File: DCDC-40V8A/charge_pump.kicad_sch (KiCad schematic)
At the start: 11 parts, among them Q23 2N7002, Q24 BSS83P, Q25 2N7002, U15 NE555D, U16 74LVC1G04

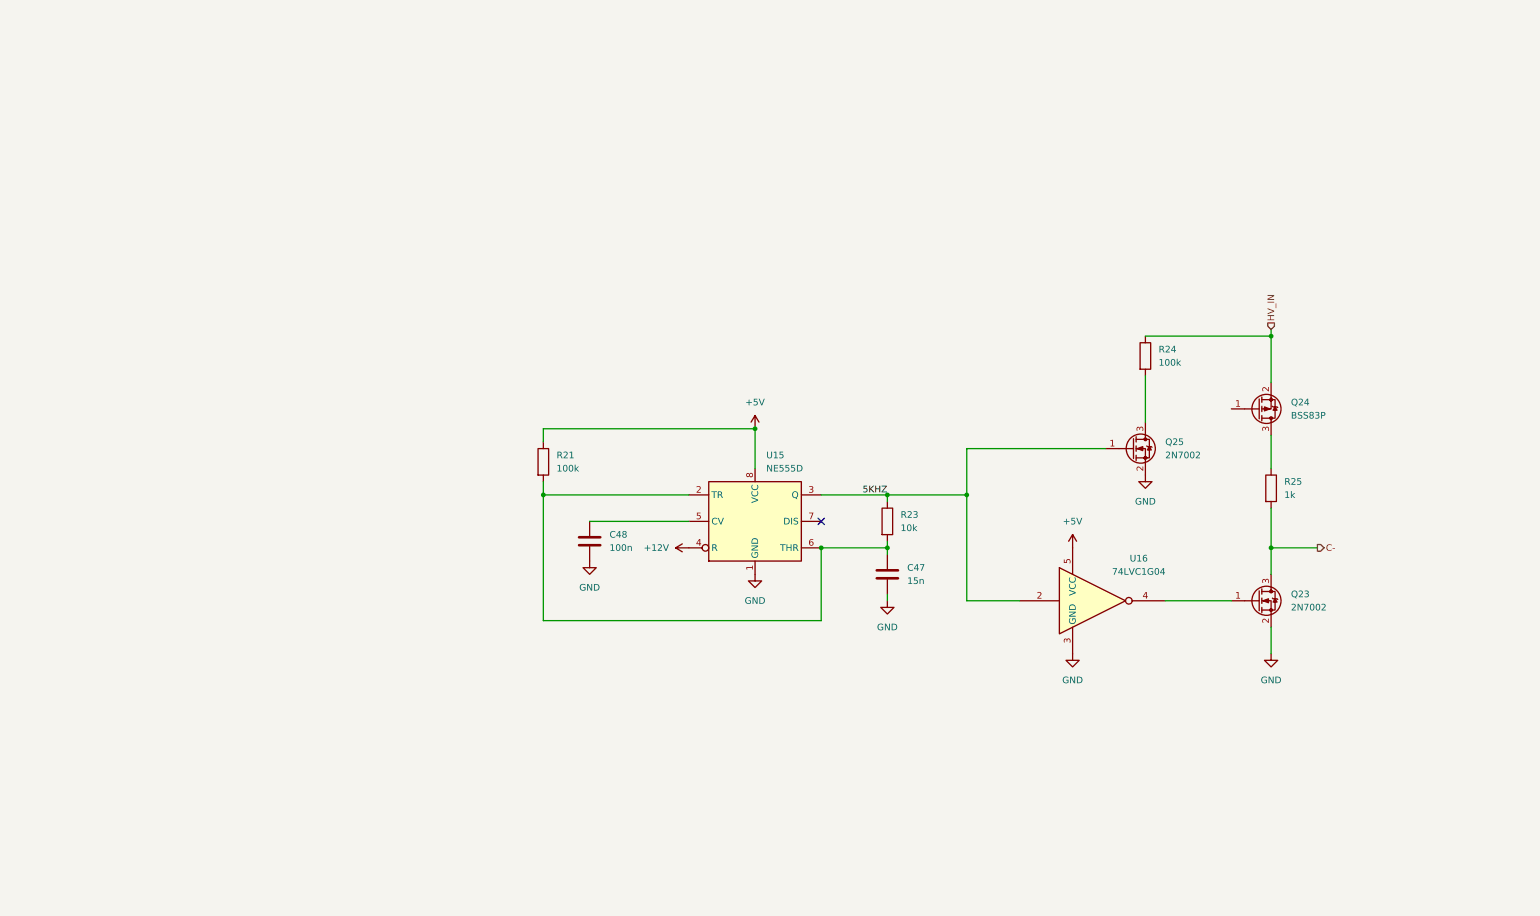
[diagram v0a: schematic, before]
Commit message: move adc MUX and discharge to new sheet
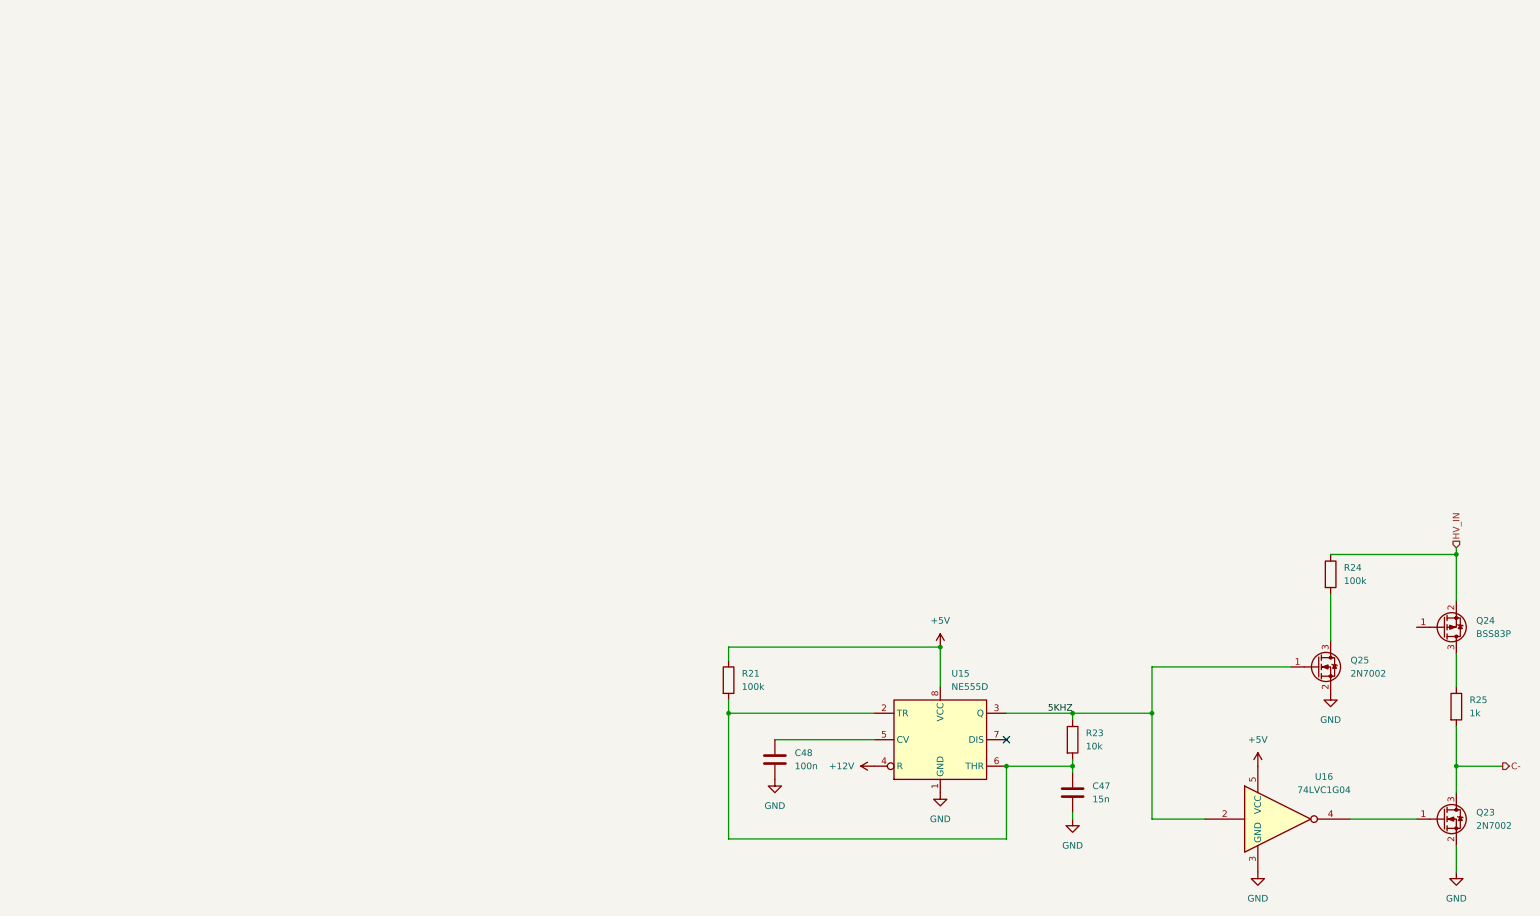
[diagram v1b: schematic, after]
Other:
- moved on the sheet: C47, C48, Q23, Q24, Q25, R21, R23, R24, R25, U15, U16

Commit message: wip
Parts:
- removed C47: 15n, Capacitor_SMD:C_0603_1608Metric, symbol Device:C
- removed C48: 100n, Capacitor_SMD:C_0603_1608Metric, symbol Device:C
- removed R21: 100k, Resistor_SMD:R_0603_1608Metric, symbol Device:R
- removed R23: 10k, Resistor_SMD:R_0603_1608Metric, symbol Device:R
- removed U15: NE555D, Package_SO:SOIC-8_3.9x4.9mm_P1.27mm, symbol Timer:NE555D
- removed U16: 74LVC1G04, Package_TO_SOT_SMD:SOT-353_SC-70-5, symbol 74xGxx:74LVC1G04
- R24: value 100k -> 10k
- R25: value 1k -> 100R
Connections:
- net C-: now also Q24.3 (D), R25.1; no longer Q23.3 (D), R25.2
- net at Q23.1 (G): now also Q24.1 (G), Q25.3 (D), R24.2
- net 5KHZ renamed PWM_IN
- net HV_IN renamed LV_IN
- new net: Q23.3 (D), R25.2
- no-connect marks 1 -> 0
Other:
- note added: "Backup:"
- moved on the sheet: Q23, Q24, R24, R25
